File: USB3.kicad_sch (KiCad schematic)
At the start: 3 parts, among them Q2302 MMBT5551

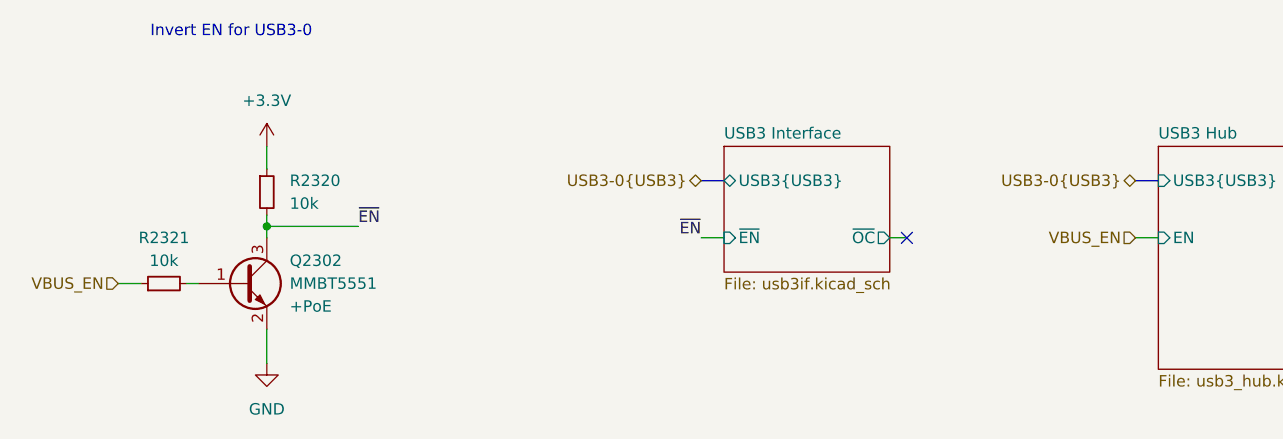
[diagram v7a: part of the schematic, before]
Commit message: Partial trace layout, kick-ass custom rules
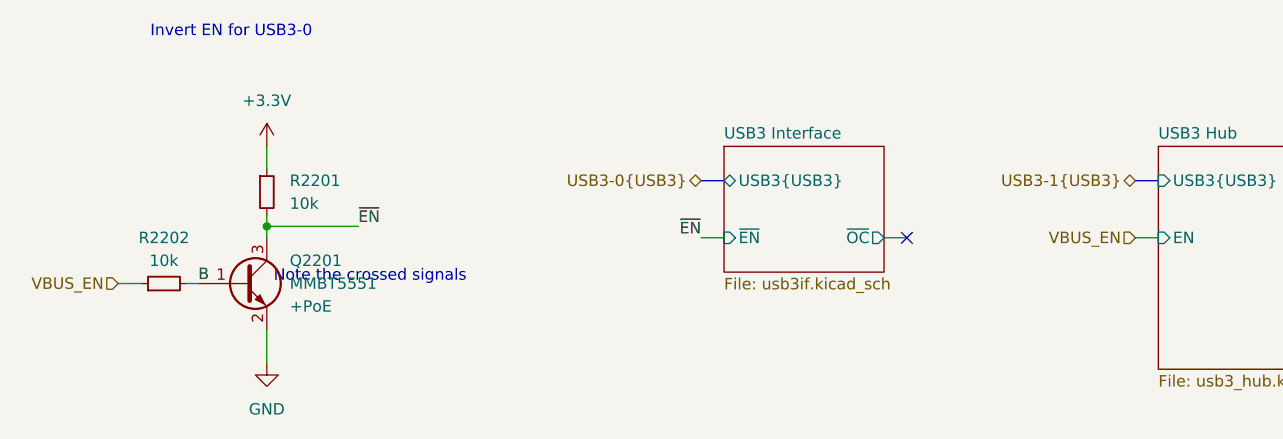
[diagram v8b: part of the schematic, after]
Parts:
- renumbered Q2302 to Q2201, R2320 to R2201, R2321 to R2202
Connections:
- net B: now reaches Q2201.1 (B), R2202.2
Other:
- note added: "Note the crossed signals"
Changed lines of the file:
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@@
-	(wire
-		(pts
-			(xy 149.225 93.98) (xy 151.13 93.98)
-		)
-		(stroke
-			(width 0)
-			(type default)
-		)
-	)
 	(wire
 		(pts
@@
 	(wire
 		(pts
+			(xy 148.59 93.98) (xy 151.13 93.98)
+		)
+		(stroke
+			(width 0)
+			(type default)
+		)
+	)
+	(wire
+		(pts
 			(xy 128.27 93.98) (xy 130.81 93.98)
 		)
@@
 			(width 0)
 			(type default)
+		)
+	)
+	(text "Note the crossed signals"
+		(exclude_from_sim no)
+		(at 80.772 98.298 0)
+		(effects
+			(font
+				(size 1.27 1.27)
+			)
+			(justify left)
 		)
 	)
@@
 		)
 	)
+	(label "B"
+		(at 72.39 99.06 0)
+		(effects
+			(font
+				(size 1.27 1.27)
+			)
+			(justify left bottom)
+		)
+	)
 	(label "~{EN}"
 		(at 90.17 92.71 0)
-		(fields_autoplaced yes)
 		(effects
 			(font
@@
 		(shape bidirectional)
 		(at 128.27 87.63 180)
-		(fields_autoplaced yes)
 		(effects
 			(font
@@
 		(shape input)
 		(at 176.53 93.98 180)
-		(fields_autoplaced yes)
 		(effects
 			(font
@@
 		(shape input)
 		(at 63.5 99.06 180)
-		(fields_autoplaced yes)
 		(effects
 			(font
@@
 		)
 	)
-	(hierarchical_label "USB3-0{USB3}"
+	(hierarchical_label "USB3-1{USB3}"
 		(shape bidirectional)
 		(at 176.53 87.63 180)
-		(fields_autoplaced yes)
 		(effects
 			(font
@@
 		(dnp no)
 		(fields_autoplaced yes)
-		(property "Reference" "Q2302"
+		(property "Reference" "Q2201"
 			(at 82.55 96.5199 0)
 			(effects
@@
 			(project "HALPI2"
 				(path "/abc482bd-3f17-4d35-80db-1da3dcdb5c27/b774f543-305e-4249-92c3-c3de7e8a285e"
-					(reference "Q2302")
+					(reference "Q2201")
 					(unit 1)
 				)
@@
 		(dnp no)
 		(fields_autoplaced yes)
-		(property "Reference" "R2320"
+		(property "Reference" "R2201"
 			(at 82.55 87.6299 0)
 			(effects
@@
 			(project ""
 				(path "/abc482bd-3f17-4d35-80db-1da3dcdb5c27/b774f543-305e-4249-92c3-c3de7e8a285e"
-					(reference "R2320")
+					(reference "R2201")
 					(unit 1)
 				)
@@
 		(dnp no)
 		(fields_autoplaced yes)
-		(property "Reference" "#PWR02335"
+		(property "Reference" "#PWR02201"
 			(at 80.01 87.63 0)
 			(effects
@@
 			(project ""
 				(path "/abc482bd-3f17-4d35-80db-1da3dcdb5c27/b774f543-305e-4249-92c3-c3de7e8a285e"
-					(reference "#PWR02335")
+					(reference "#PWR02201")
 					(unit 1)
 				)
@@
 		(dnp no)
 		(fields_autoplaced yes)
-		(property "Reference" "#PWR02334"
+		(property "Reference" "#PWR02202"
 			(at 80.01 114.3 0)
 			(effects
@@
 			(project ""
 				(path "/abc482bd-3f17-4d35-80db-1da3dcdb5c27/b774f543-305e-4249-92c3-c3de7e8a285e"
-					(reference "#PWR02334")
+					(reference "#PWR02202")
 					(unit 1)
 				)
@@
 		(dnp no)
 		(fields_autoplaced yes)
-		(property "Reference" "R2321"
+		(property "Reference" "R2202"
 			(at 68.58 93.98 90)
 			(effects
@@
 			(project "HALPI2"
 				(path "/abc482bd-3f17-4d35-80db-1da3dcdb5c27/b774f543-305e-4249-92c3-c3de7e8a285e"
-					(reference "R2321")
+					(reference "R2202")
 					(unit 1)
 				)
@@
 	(sheet
 		(at 130.81 83.82)
-		(size 18.415 13.97)
+		(size 17.78 13.97)
 		(fields_autoplaced yes)
 		(stroke
@@
 		)
 		(pin "~{OC}" output
-			(at 149.225 93.98 0)
-			(effects
-				(font
+			(at 148.59 93.98 0)
+			(effects
+				(font
